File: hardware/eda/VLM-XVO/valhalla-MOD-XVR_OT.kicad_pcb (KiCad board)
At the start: 2 copper layers, 76.2 x 50.8 mm, 5 parts, among them J1 BUS

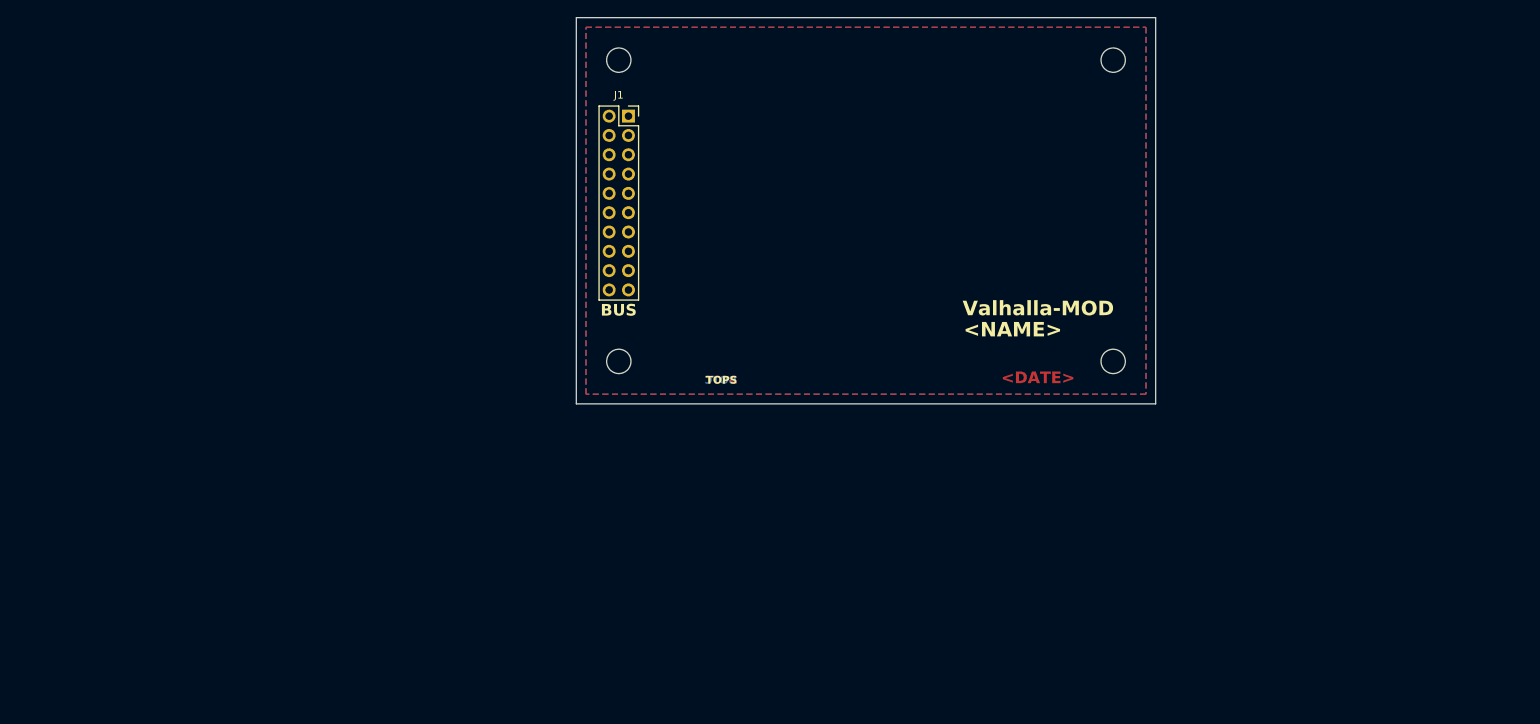
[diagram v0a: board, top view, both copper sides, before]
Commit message: UPDATE: progress on XVR(GPIO-OT-I)
  - full opto-isolation on all GPIOs
  - buffering on all GPIOs driving the LED side of the optocouplers
  - began layout work, this is either going to be a tight or a large
    one.
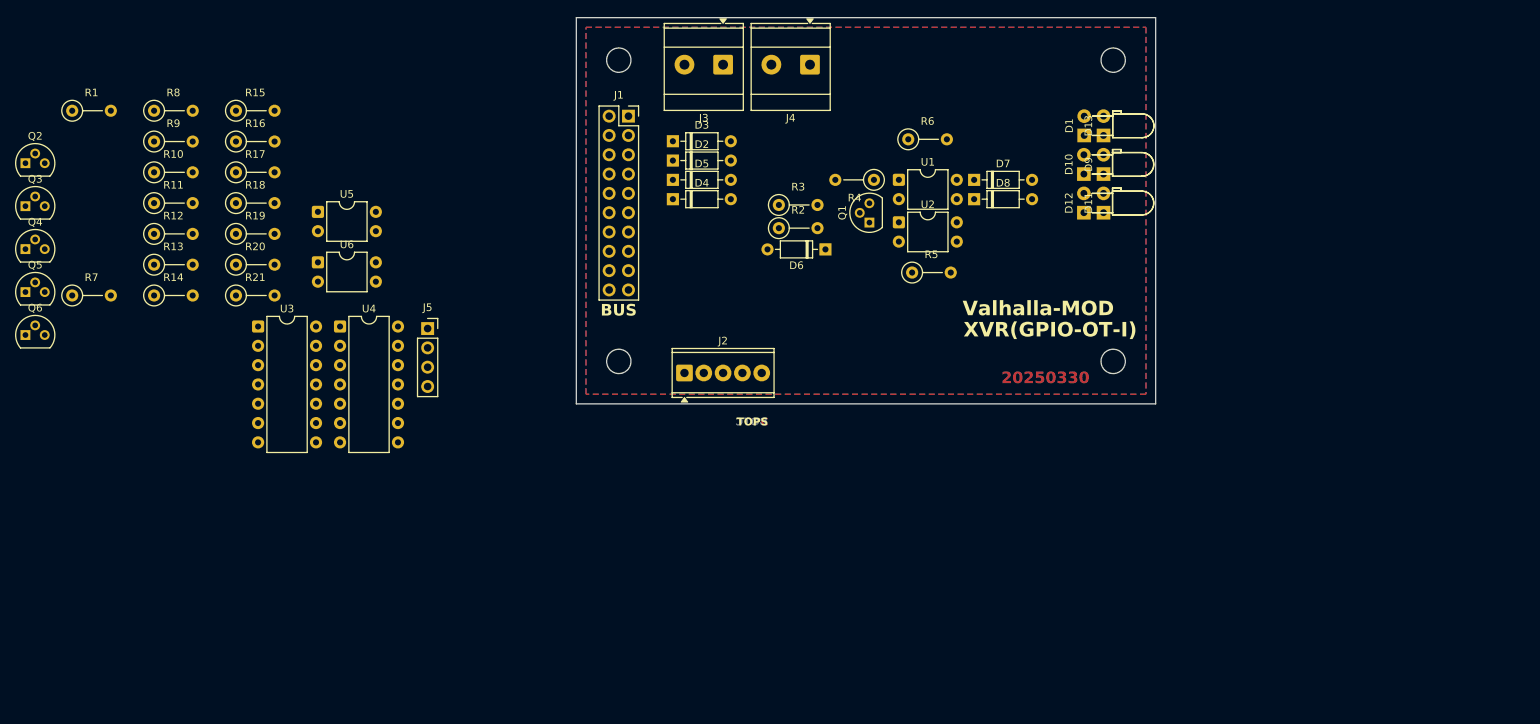
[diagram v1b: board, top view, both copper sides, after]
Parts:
- added D1: R, LED_THT:LED_D3.0mm_Horizontal_O3.81mm_Z6.0mm, F.Cu at (135.4, 51.1)
- added D10: R, LED_THT:LED_D3.0mm_Horizontal_O3.81mm_Z6.0mm, F.Cu at (135.3, 56.1)
- added D11: R, LED_THT:LED_D3.0mm_Horizontal_O1.27mm_Z2.0mm, F.Cu at (137.9, 61.2)
- added D12: R, LED_THT:LED_D3.0mm_Horizontal_O3.81mm_Z6.0mm, F.Cu at (135.3, 61.2)
- added D13: R, LED_THT:LED_D3.0mm_Horizontal_O1.27mm_Z2.0mm, F.Cu at (137.9, 51.1)
- added D2: 1N4148, Diode_THT:D_DO-35_SOD27_P7.62mm_Horizontal, F.Cu at (81.3, 54.4)
- added D3: 1N4148, Diode_THT:D_DO-35_SOD27_P7.62mm_Horizontal, F.Cu at (81.3, 51.8)
- added D4: 1N4148, Diode_THT:D_DO-35_SOD27_P7.62mm_Horizontal, F.Cu at (81.3, 59.4)
- added D5: 1N4148, Diode_THT:D_DO-35_SOD27_P7.62mm_Horizontal, F.Cu at (81.3, 56.9)
- added D6: 4V7, Diode_THT:D_DO-35_SOD27_P7.62mm_Horizontal, F.Cu at (101.3, 66.0)
- added D7: 13V, Diode_THT:D_DO-35_SOD27_P7.62mm_Horizontal, F.Cu at (120.9, 56.9)
- added D8: 4V3, Diode_THT:D_DO-35_SOD27_P7.62mm_Horizontal, F.Cu at (120.9, 59.4)
- added D9: R, LED_THT:LED_D3.0mm_Horizontal_O1.27mm_Z2.0mm, F.Cu at (137.9, 56.1)
- added J2: GPIO, TerminalBlock_Phoenix:TerminalBlock_Phoenix_MPT-0,5-5-2.54_1x05_P2.54mm_Horizontal, F.Cu at (82.8, 82.3)
- added J3: OT+_Boiler, TerminalBlock_Phoenix:TerminalBlock_Phoenix_MKDS-3-2-5.08_1x02_P5.08mm_Horizontal, F.Cu at (87.9, 41.7)
- added J4: OT+_Thermostat, TerminalBlock_Phoenix:TerminalBlock_Phoenix_MKDS-3-2-5.08_1x02_P5.08mm_Horizontal, F.Cu at (99.3, 41.7)
- added J5: 24V_BOOST, Connector_PinSocket_2.54mm:PinSocket_1x04_P2.54mm_Vertical, F.Cu at (49.0, 76.5)
- added Q1: BC558, Package_TO_SOT_THT:TO-92L, F.Cu at (107.1, 62.5)
- added Q2: BC558, Package_TO_SOT_THT:TO-92L, F.Cu at (-3.88, 54.7)
- added Q3: BC558, Package_TO_SOT_THT:TO-92L, F.Cu at (-3.88, 60.4)
- added Q4: BC558, Package_TO_SOT_THT:TO-92L, F.Cu at (-3.88, 66.0)
- added Q5: BC548, Package_TO_SOT_THT:TO-92L, F.Cu at (-3.88, 71.7)
- added Q6: BC548, Package_TO_SOT_THT:TO-92L, F.Cu at (-3.88, 77.3)
- added R1: R, Resistor_THT:R_Axial_DIN0207_L6.3mm_D2.5mm_P5.08mm_Vertical, F.Cu at (2.27, 47.8)
- added R10: R, Resistor_THT:R_Axial_DIN0207_L6.3mm_D2.5mm_P5.08mm_Vertical, F.Cu at (13.0, 55.9)
- added R11: 33K, Resistor_THT:R_Axial_DIN0207_L6.3mm_D2.5mm_P5.08mm_Vertical, F.Cu at (13.0, 60.0)
- added R12: 100R, Resistor_THT:R_Axial_DIN0207_L6.3mm_D2.5mm_P5.08mm_Vertical, F.Cu at (13.0, 64.0)
- added R13: 39R, Resistor_THT:R_Axial_DIN0207_L6.3mm_D2.5mm_P5.08mm_Vertical, F.Cu at (13.0, 68.1)
- added R14: 20K, Resistor_THT:R_Axial_DIN0207_L6.3mm_D2.5mm_P5.08mm_Vertical, F.Cu at (13.0, 72.1)
- added R15: 10K, Resistor_THT:R_Axial_DIN0207_L6.3mm_D2.5mm_P5.08mm_Vertical, F.Cu at (23.8, 47.8)
- added R16: R, Resistor_THT:R_Axial_DIN0207_L6.3mm_D2.5mm_P5.08mm_Vertical, F.Cu at (23.8, 51.9)
- added R17: 1K, Resistor_THT:R_Axial_DIN0207_L6.3mm_D2.5mm_P5.08mm_Vertical, F.Cu at (23.8, 55.9)
- added R18: 4K7, Resistor_THT:R_Axial_DIN0207_L6.3mm_D2.5mm_P5.08mm_Vertical, F.Cu at (23.8, 60.0)
- added R19: 330, Resistor_THT:R_Axial_DIN0207_L6.3mm_D2.5mm_P5.08mm_Vertical, F.Cu at (23.8, 64.0)
- added R2: 220R, Resistor_THT:R_Axial_DIN0207_L6.3mm_D2.5mm_P5.08mm_Vertical, F.Cu at (95.2, 63.2)
- added R20: 10K, Resistor_THT:R_Axial_DIN0207_L6.3mm_D2.5mm_P5.08mm_Vertical, F.Cu at (23.8, 68.1)
- added R21: 330R, Resistor_THT:R_Axial_DIN0207_L6.3mm_D2.5mm_P5.08mm_Vertical, F.Cu at (23.8, 72.1)
- added R3: 100R, Resistor_THT:R_Axial_DIN0207_L6.3mm_D2.5mm_P5.08mm_Vertical, F.Cu at (95.2, 60.2)
- added R4: 330R, Resistor_THT:R_Axial_DIN0207_L6.3mm_D2.5mm_P5.08mm_Vertical, F.Cu at (107.7, 56.9)
- added R5: 10K, Resistor_THT:R_Axial_DIN0207_L6.3mm_D2.5mm_P5.08mm_Vertical, F.Cu at (112.7, 69.1)
- added R6: 330R, Resistor_THT:R_Axial_DIN0207_L6.3mm_D2.5mm_P5.08mm_Vertical, F.Cu at (112.2, 51.6)
- added R7: R, Resistor_THT:R_Axial_DIN0207_L6.3mm_D2.5mm_P5.08mm_Vertical, F.Cu at (2.27, 72.1)
- added R8: R, Resistor_THT:R_Axial_DIN0207_L6.3mm_D2.5mm_P5.08mm_Vertical, F.Cu at (13.0, 47.8)
- added R9: R, Resistor_THT:R_Axial_DIN0207_L6.3mm_D2.5mm_P5.08mm_Vertical, F.Cu at (13.0, 51.9)
- added U1: PC817, Package_DIP:DIP-4_W7.62mm, F.Cu at (111.0, 56.9)
- added U2: PC817, Package_DIP:DIP-4_W7.62mm, F.Cu at (111.0, 62.5)
- added U3: 74LS06, Package_DIP:DIP-14_W7.62mm, F.Cu at (26.7, 76.2)
- added U4: 74LS07, Package_DIP:DIP-14_W7.62mm, F.Cu at (37.5, 76.2)
- added U5: PC817, Package_DIP:DIP-4_W7.62mm, F.Cu at (34.6, 61.1)
- added U6: PC817, Package_DIP:DIP-4_W7.62mm, F.Cu at (34.6, 67.7)
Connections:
- J1 pad 1: /AVCC -> unconnected-(J1-Pin_1-Pad1)
- J1 pad 10: /~{SS} -> unconnected-(J1-Pin_10-Pad10)
- J1 pad 11: /~{SINT} -> unconnected-(J1-Pin_11-Pad11)
- J1 pad 13: /SDA -> unconnected-(J1-Pin_13-Pad13)
- J1 pad 14: /SCL -> unconnected-(J1-Pin_14-Pad14)
- J1 pad 15: /~{IINT} -> unconnected-(J1-Pin_15-Pad15)
- J1 pad 16: unconnected-(J1-Pin_16-Pad16) -> /LVCC
- J1 pad 17: /RXDI -> unconnected-(J1-Pin_17-Pad17)
- J1 pad 18: /TXDO -> unconnected-(J1-Pin_18-Pad18)
- J1 pad 19: /~{RTS} -> unconnected-(J1-Pin_19-Pad19)
- J1 pad 2: /AGND -> unconnected-(J1-Pin_2-Pad2)
- J1 pad 20: /~{DCD} -> unconnected-(J1-Pin_20-Pad20)
- J1 pad 5: /~{RESET} -> unconnected-(J1-Pin_5-Pad5)
- J1 pad 6: unconnected-(J1-Pin_6-Pad6) -> /DGND
- J1 pad 7: /MOSI -> unconnected-(J1-Pin_7-Pad7)
- J1 pad 8: /MISO -> unconnected-(J1-Pin_8-Pad8)
- J1 pad 9: /SCK -> unconnected-(J1-Pin_9-Pad9)
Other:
- board text added: "20250330"
- board text added: "XVR(GPIO-OT-I)"
- board text removed: "<DATE>"
- board text removed: "<NAME>"

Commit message: UPDATE: minor progress on layout of MOD-XVR(GPIO-OT-I)
  - bulk-grouped by functional blocks, it might all fit afterall.
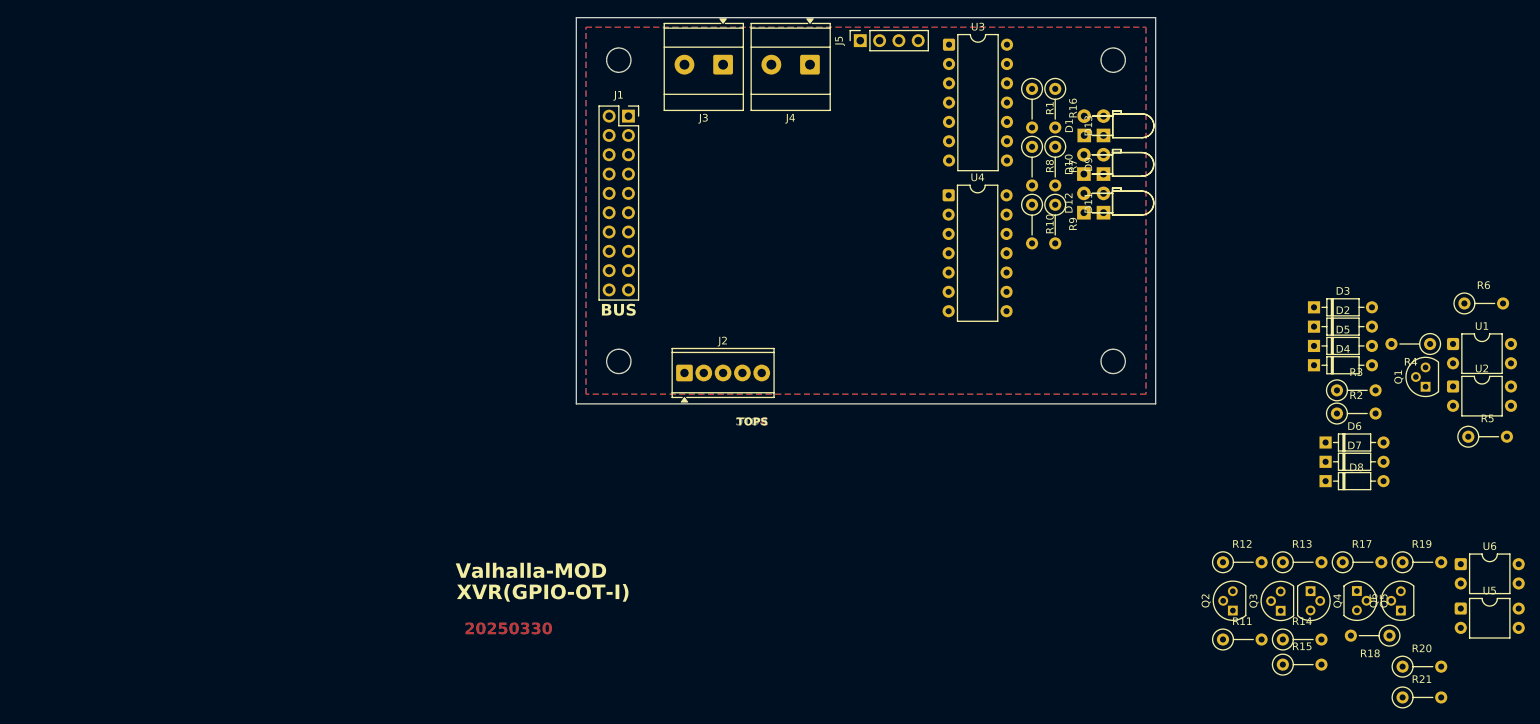
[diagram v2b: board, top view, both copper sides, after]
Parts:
- moved Q6 184.5 mm to (177.0, 113.5), turned to 90 degrees
- moved Q5 179.5 mm to (171.2, 111.0), turned to -90 degrees
- moved Q4 174.9 mm to (165.2, 111.0), turned to -90 degrees
- moved Q3 173.5 mm to (161.2, 113.6), turned to 90 degrees
- moved Q2 169.4 mm to (154.9, 113.5), turned to 90 degrees
- moved R20 162.3 mm to (177.3, 120.9)
- moved R21 162.3 mm to (177.3, 125.0)
- moved R18 162.0 mm to (175.5, 116.8), turned to 180 degrees
- moved R19 159.4 mm to (177.3, 107.2)
- moved U5 159.1 mm to (184.9, 113.3)
- moved R15 155.8 mm to (161.5, 120.7)
- moved U6 155.5 mm to (184.9, 107.4)
- moved R14 155.2 mm to (161.5, 117.4)
- moved R17 154.3 mm to (169.4, 107.2)
- moved R13 153.5 mm to (161.5, 107.2)
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
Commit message: UPDATE: further progress with layout of MOD-XVR(OT+)
  - thermostat section done as a group
  - boiler section to follow
  - connections to the rest of the circuit go last.
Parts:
- moved Q6 91.9 mm to (93.2, 76.0)
- moved R21 89.2 mm to (106.7, 70.4), turned to 90 degrees
- moved R18 85.6 mm to (103.6, 70.4), turned to 90 degrees
- moved U5 85.3 mm to (105.9, 81.0)
- moved U6 85.3 mm to (105.9, 75.2)
- moved R19 85.1 mm to (100.6, 70.4), turned to 90 degrees
- moved R14 84.4 mm to (91.4, 70.4), turned to 90 degrees
- moved R20 84.4 mm to (109.7, 70.4), turned to 90 degrees
- moved R17 83.5 mm to (94.5, 70.4), turned to 90 degrees
- moved R11 82.9 mm to (85.3, 70.4), turned to 90 degrees
- moved Q3 82.0 mm to (88.4, 76.0)
- moved R13 81.9 mm to (88.4, 70.4), turned to 90 degrees
- moved R15 81.4 mm to (97.5, 70.4), turned to 90 degrees
- moved Q2 80.7 mm to (83.6, 76.0)
- moved R12 80.3 mm to (82.3, 70.4), turned to 90 degrees
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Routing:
- net Net-(Q4-C): track 0.00 -> 24.4 mm
- net Net-(R18-Pad1): track 0.00 -> 20.6 mm, vias 0 -> 1
- net /OVCC: track 0.00 -> 19.5 mm
- net Net-(Q2-B): track 0.00 -> 17.9 mm
- net Net-(Q6-B): track 0.00 -> 17.1 mm
- net Net-(R19-Pad2): track 0.00 -> 15.7 mm
- net Net-(Q6-E): track 0.00 -> 15.5 mm
- net /OTT_TXDI: track 0.00 -> 14.0 mm
- net Net-(R21-Pad1): track 0.00 -> 11.6 mm
- net Net-(Q2-C): track 0.00 -> 9.14 mm
- net Net-(Q5-E): track 0.00 -> 8.72 mm
- net Net-(D1-A): track 0.00 -> 8.34 mm
- net Net-(D10-A): track 0.00 -> 8.00 mm
- net Net-(D13-A): track 0.00 -> 7.83 mm
- net Net-(D12-A): track 0.00 -> 7.44 mm
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
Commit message: UPDATE: MOD-XVR(OT+) net layout complete!
  - it finally all fit in, with some small room to spare
  - silkscreen is next.
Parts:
- moved R6 90.9 mm to (92.5, 56.4), turned to -90 degrees
- moved D4 81.5 mm to (82.0, 62.7), turned to 90 degrees
- moved D2 79.4 mm to (84.6, 62.7), turned to 90 degrees
- moved U1 77.4 mm to (105.9, 38.6)
- moved U2 77.3 mm to (105.9, 44.4)
- moved Q1 76.8 mm to (101.9, 50.0), turned to -90 degrees
- moved D5 76.6 mm to (87.1, 62.7), turned to 90 degrees
- moved D3 74.8 mm to (89.7, 62.7), turned to 90 degrees
- moved R5 72.1 mm to (112.3, 56.4), turned to -90 degrees
- moved R4 71.9 mm to (106.7, 56.4), turned to -90 degrees
- moved R3 71.0 mm to (95.5, 56.4), turned to -90 degrees
- moved D6 66.7 mm to (98.3, 62.7), turned to 90 degrees
- moved R2 65.7 mm to (101.1, 56.4), turned to -90 degrees
- moved D7 61.4 mm to (103.9, 62.7), turned to 90 degrees
- moved D8 56.3 mm to (109.5, 62.7), turned to 90 degrees
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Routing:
- net /LVCC: track 0.00 -> 98.1 mm, vias 0 -> 2
- net /OVCC: track 19.5 -> 99.2 mm
- net /OTB_RXDO: track 0.00 -> 76.7 mm, vias 0 -> 1
- net /OTB_TXDI: track 0.00 -> 72.3 mm, vias 0 -> 1
- net /~{OVCC_EN}: track 0.00 -> 71.1 mm, vias 0 -> 2
- net /OTT_RXDO: track 0.00 -> 59.4 mm
- net /OTT_TXDI: track 14.0 -> 67.3 mm, vias 0 -> 2
- net Net-(D13-K): track 0.00 -> 40.9 mm, vias 0 -> 1
- net /OTB_RXDO_B: track 0.00 -> 39.5 mm, vias 0 -> 1
- net Net-(D2-K): track 0.00 -> 36.5 mm, vias 0 -> 1
- net Net-(D7-K): track 0.00 -> 33.6 mm, vias 0 -> 1
- net Net-(D9-K): track 0.00 -> 33.2 mm, vias 0 -> 1
- net Net-(J4-Pin_1): track 6.86 -> 39.7 mm
- net Net-(D3-A): track 0.00 -> 32.4 mm
- net Net-(D11-K): track 0.00 -> 31.3 mm, vias 0 -> 1
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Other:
- board text added: "XVR(OT+)"
- board text removed: "XVR(GPIO-OT-I)"

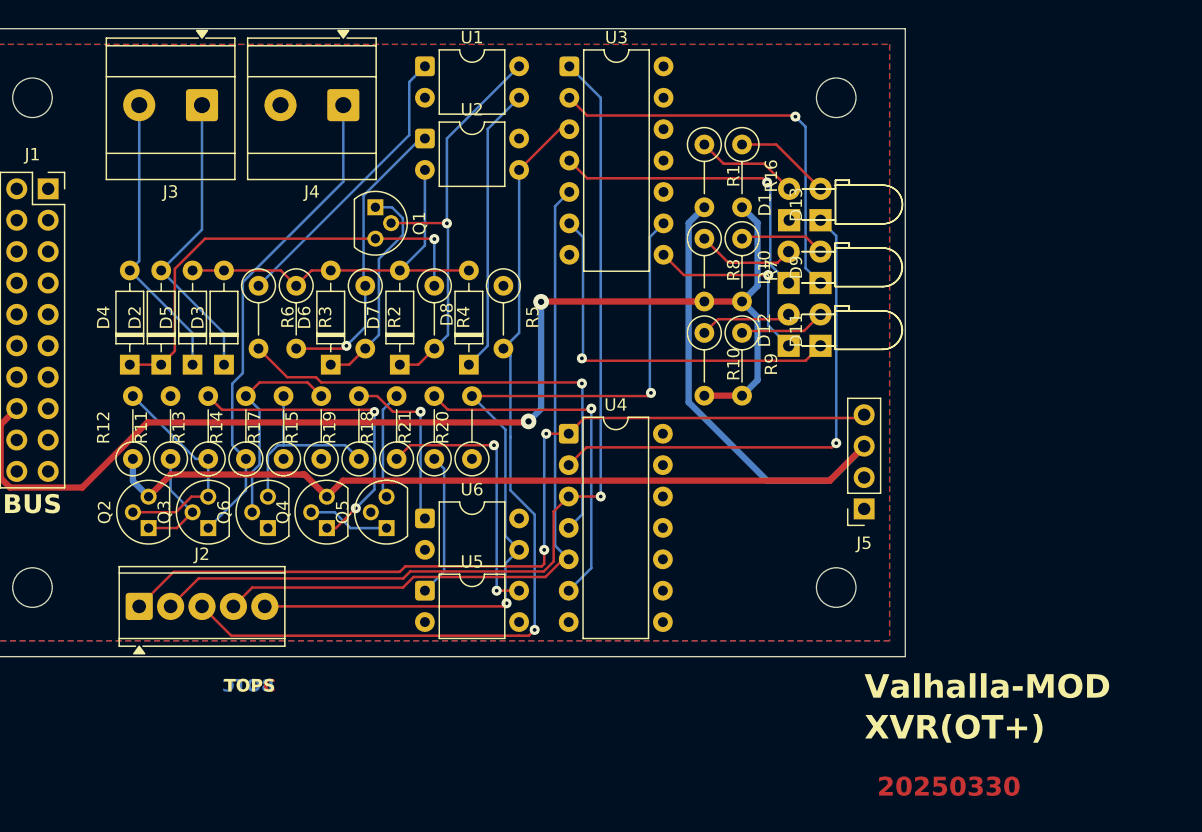
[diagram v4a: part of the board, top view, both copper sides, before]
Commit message: UPDATE: MOD-XVR(OT+) layout complete, RTM!
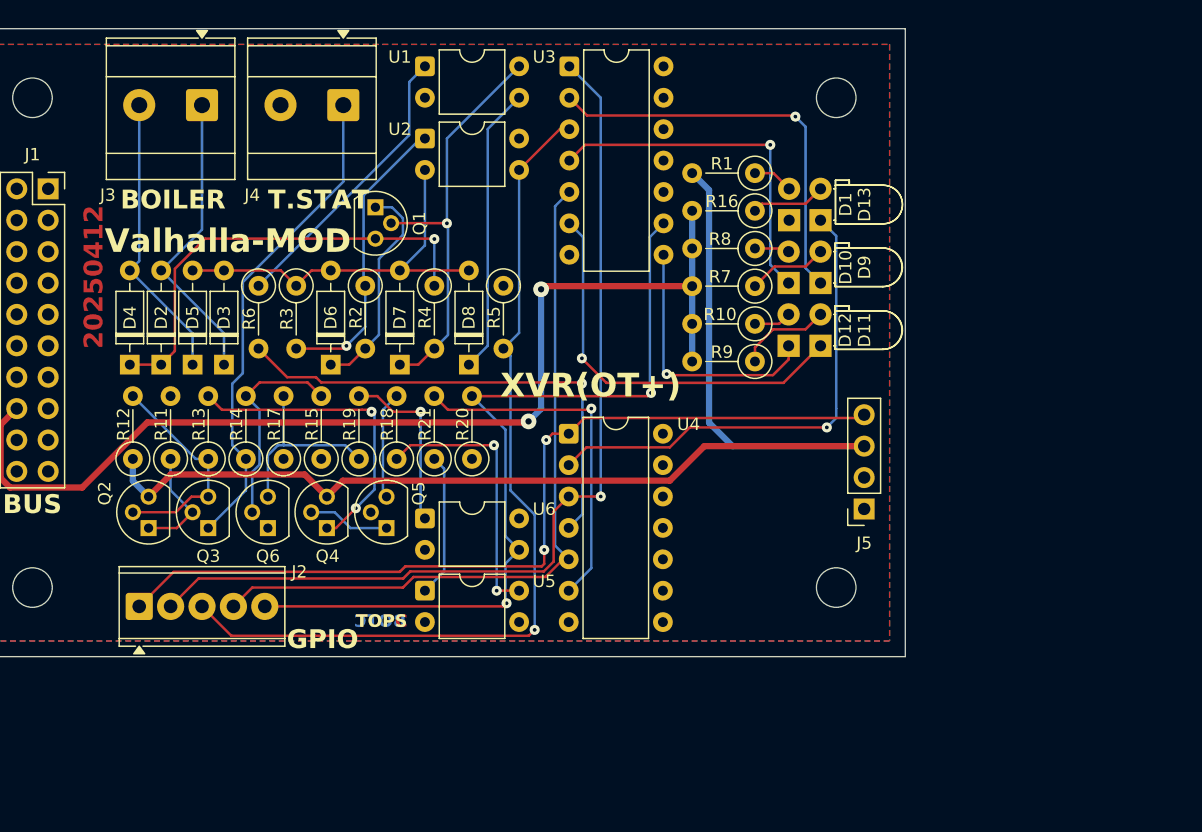
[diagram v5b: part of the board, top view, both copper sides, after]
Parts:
- moved R16 5.46 mm to (132.6, 50.3), turned to 180 degrees
- moved R1 4.70 mm to (132.6, 47.2), turned to 180 degrees
- moved R8 4.17 mm to (132.6, 53.3), turned to 180 degrees
- moved R10 4.16 mm to (132.6, 59.4), turned to 180 degrees
- moved R7 3.98 mm to (132.6, 56.4), turned to 180 degrees
- moved R9 2.54 mm to (132.6, 62.5), turned to 180 degrees
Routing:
- net /LVCC: track 98.1 -> 87.0 mm
- net Net-(D12-K): track 15.6 -> 21.3 mm
- net Net-(D10-A): track 8.00 -> 2.83 mm
- net Net-(D1-A): track 8.34 -> 3.29 mm
- net Net-(D12-A): track 7.44 -> 3.04 mm
- net Net-(D10-K): track 25.6 -> 28.6 mm
- net Net-(D13-A): track 7.83 -> 6.04 mm
- net Net-(D11-K): track 31.3 -> 32.8 mm
- net Net-(D13-K): track 40.9 -> 39.7 mm
- net /~{OVCC_EN}: track 71.1 -> 70.5 mm
- net Net-(D11-A): track 6.97 -> 7.55 mm
- net Net-(R2-Pad1): track 23.9 -> 23.3 mm
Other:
- board text added: "20250412"
- board text added: "BOILER"
- board text added: "GPIO"
- board text added: "T.STAT"
- board text removed: "20250330"
